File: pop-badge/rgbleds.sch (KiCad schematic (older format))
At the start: 25 parts, among them U1 WS2812-2020, U10 WS2812-2020, U11 WS2812-2020, U12 WS2812-2020, U13 WS2812-2020, U14 WS2812-2020, U15 WS2812-2020, U16 WS2812-2020, U17 WS2812-2020, U18 WS2812-2020, U19 WS2812-2020, U2 WS2812-2020, U20 WS2812-2020, U21 WS2812-2020, U22 WS2812-2020, U23 WS2812-2020, U24 WS2812-2020, U25 WS2812-2020, U3 WS2812-2020, U4 WS2812-2020, U5 WS2812-2020, U6 WS2812-2020, U7 WS2812-2020, U8 WS2812-2020, U9 WS2812-2020

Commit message: routing mostly done
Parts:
- U1, U10, U11, U12, U13, U14, U15, U16, U17, U18, U19, U2, U20, U21, U22, U23, U24, U25, U3, U4, U5, U6, U7, U8, U9: JLC (none) -> C965555
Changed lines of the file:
@@
 F 4 "Manufacturer Recommendations" H 2850 1200 50  0001 L BNN "STANDARD"
 F 5 "Worldsemi" H 2850 1200 50  0001 L BNN "MANUFACTURER"
+F 6 "C965555" H 2850 1200 50  0001 C CNN "JLC"
+F 7 "" H 2850 1200 50  0001 C CNN "LCSC"
 	1    2850 1200
 	1    0    0    -1
@@
 F 4 "Manufacturer Recommendations" H 4250 1200 50  0001 L BNN "STANDARD"
 F 5 "Worldsemi" H 4250 1200 50  0001 L BNN "MANUFACTURER"
+F 6 "C965555" H 4250 1200 50  0001 C CNN "JLC"
 	1    4250 1200
 	1    0    0    -1
@@
 F 4 "Manufacturer Recommendations" H 5650 1200 50  0001 L BNN "STANDARD"
 F 5 "Worldsemi" H 5650 1200 50  0001 L BNN "MANUFACTURER"
+F 6 "C965555" H 5650 1200 50  0001 C CNN "JLC"
 	1    5650 1200
 	1    0    0    -1
@@
 F 4 "Manufacturer Recommendations" H 7050 1200 50  0001 L BNN "STANDARD"
 F 5 "Worldsemi" H 7050 1200 50  0001 L BNN "MANUFACTURER"
+F 6 "C965555" H 7050 1200 50  0001 C CNN "JLC"
 	1    7050 1200
 	1    0    0    -1
@@
 F 4 "Manufacturer Recommendations" H 2850 2450 50  0001 L BNN "STANDARD"
 F 5 "Worldsemi" H 2850 2450 50  0001 L BNN "MANUFACTURER"
+F 6 "C965555" H 2850 2450 50  0001 C CNN "JLC"
 	1    2850 2450
 	1    0    0    -1
@@
 F 4 "Manufacturer Recommendations" H 4250 2450 50  0001 L BNN "STANDARD"
 F 5 "Worldsemi" H 4250 2450 50  0001 L BNN "MANUFACTURER"
+F 6 "C965555" H 4250 2450 50  0001 C CNN "JLC"
 	1    4250 2450
 	1    0    0    -1
@@
 F 4 "Manufacturer Recommendations" H 5650 2450 50  0001 L BNN "STANDARD"
 F 5 "Worldsemi" H 5650 2450 50  0001 L BNN "MANUFACTURER"
+F 6 "C965555" H 5650 2450 50  0001 C CNN "JLC"
 	1    5650 2450
 	1    0    0    -1
@@
 F 4 "Manufacturer Recommendations" H 7050 2450 50  0001 L BNN "STANDARD"
 F 5 "Worldsemi" H 7050 2450 50  0001 L BNN "MANUFACTURER"
+F 6 "C965555" H 7050 2450 50  0001 C CNN "JLC"
 	1    7050 2450
 	1    0    0    -1
@@
 F 4 "Manufacturer Recommendations" H 8450 2450 50  0001 L BNN "STANDARD"
 F 5 "Worldsemi" H 8450 2450 50  0001 L BNN "MANUFACTURER"
+F 6 "C965555" H 8450 2450 50  0001 C CNN "JLC"
 	1    8450 2450
 	1    0    0    -1
@@
 F 4 "Manufacturer Recommendations" H 2850 3650 50  0001 L BNN "STANDARD"
 F 5 "Worldsemi" H 2850 3650 50  0001 L BNN "MANUFACTURER"
+F 6 "C965555" H 2850 3650 50  0001 C CNN "JLC"
 	1    2850 3650
 	1    0    0    -1
@@
 F 4 "Manufacturer Recommendations" H 4250 3650 50  0001 L BNN "STANDARD"
 F 5 "Worldsemi" H 4250 3650 50  0001 L BNN "MANUFACTURER"
+F 6 "C965555" H 4250 3650 50  0001 C CNN "JLC"
 	1    4250 3650
 	1    0    0    -1
@@
 F 4 "Manufacturer Recommendations" H 5650 3650 50  0001 L BNN "STANDARD"
 F 5 "Worldsemi" H 5650 3650 50  0001 L BNN "MANUFACTURER"
+F 6 "C965555" H 5650 3650 50  0001 C CNN "JLC"
 	1    5650 3650
 	1    0    0    -1
@@
 F 4 "Manufacturer Recommendations" H 7050 3650 50  0001 L BNN "STANDARD"
 F 5 "Worldsemi" H 7050 3650 50  0001 L BNN "MANUFACTURER"
+F 6 "C965555" H 7050 3650 50  0001 C CNN "JLC"
 	1    7050 3650
 	1    0    0    -1
@@
 F 4 "Manufacturer Recommendations" H 8450 3650 50  0001 L BNN "STANDARD"
 F 5 "Worldsemi" H 8450 3650 50  0001 L BNN "MANUFACTURER"
+F 6 "C965555" H 8450 3650 50  0001 C CNN "JLC"
 	1    8450 3650
 	1    0    0    -1
@@
 F 4 "Manufacturer Recommendations" H 2850 4800 50  0001 L BNN "STANDARD"
 F 5 "Worldsemi" H 2850 4800 50  0001 L BNN "MANUFACTURER"
+F 6 "C965555" H 2850 4800 50  0001 C CNN "JLC"
 	1    2850 4800
 	1    0    0    -1
@@
 F 4 "Manufacturer Recommendations" H 4250 4800 50  0001 L BNN "STANDARD"
 F 5 "Worldsemi" H 4250 4800 50  0001 L BNN "MANUFACTURER"
+F 6 "C965555" H 4250 4800 50  0001 C CNN "JLC"
 	1    4250 4800
 	1    0    0    -1
@@
 F 4 "Manufacturer Recommendations" H 5650 4800 50  0001 L BNN "STANDARD"
 F 5 "Worldsemi" H 5650 4800 50  0001 L BNN "MANUFACTURER"
+F 6 "C965555" H 5650 4800 50  0001 C CNN "JLC"
 	1    5650 4800
 	1    0    0    -1
@@
 F 4 "Manufacturer Recommendations" H 7050 4800 50  0001 L BNN "STANDARD"
 F 5 "Worldsemi" H 7050 4800 50  0001 L BNN "MANUFACTURER"
+F 6 "C965555" H 7050 4800 50  0001 C CNN "JLC"
 	1    7050 4800
 	1    0    0    -1
@@
 F 4 "Manufacturer Recommendations" H 8450 4800 50  0001 L BNN "STANDARD"
 F 5 "Worldsemi" H 8450 4800 50  0001 L BNN "MANUFACTURER"
+F 6 "C965555" H 8450 4800 50  0001 C CNN "JLC"
 	1    8450 4800
 	1    0    0    -1
@@
 F 4 "Manufacturer Recommendations" H 2850 5950 50  0001 L BNN "STANDARD"
 F 5 "Worldsemi" H 2850 5950 50  0001 L BNN "MANUFACTURER"
+F 6 "C965555" H 2850 5950 50  0001 C CNN "JLC"
 	1    2850 5950
 	1    0    0    -1
@@
 F 4 "Manufacturer Recommendations" H 4250 5950 50  0001 L BNN "STANDARD"
 F 5 "Worldsemi" H 4250 5950 50  0001 L BNN "MANUFACTURER"
+F 6 "C965555" H 4250 5950 50  0001 C CNN "JLC"
 	1    4250 5950
 	1    0    0    -1
@@
 F 4 "Manufacturer Recommendations" H 5650 5950 50  0001 L BNN "STANDARD"
 F 5 "Worldsemi" H 5650 5950 50  0001 L BNN "MANUFACTURER"
+F 6 "C965555" H 5650 5950 50  0001 C CNN "JLC"
 	1    5650 5950
 	1    0    0    -1
@@
 F 4 "Manufacturer Recommendations" H 7050 5950 50  0001 L BNN "STANDARD"
 F 5 "Worldsemi" H 7050 5950 50  0001 L BNN "MANUFACTURER"
+F 6 "C965555" H 7050 5950 50  0001 C CNN "JLC"
 	1    7050 5950
 	1    0    0    -1
@@
 F 4 "Manufacturer Recommendations" H 8450 5950 50  0001 L BNN "STANDARD"
 F 5 "Worldsemi" H 8450 5950 50  0001 L BNN "MANUFACTURER"
+F 6 "C965555" H 8450 5950 50  0001 C CNN "JLC"
 	1    8450 5950
 	1    0    0    -1
@@
 F 4 "Manufacturer Recommendations" H 8450 1200 50  0001 L BNN "STANDARD"
 F 5 "Worldsemi" H 8450 1200 50  0001 L BNN "MANUFACTURER"
+F 6 "C965555" H 8450 1200 50  0001 C CNN "JLC"
 	1    8450 1200
 	1    0    0    -1

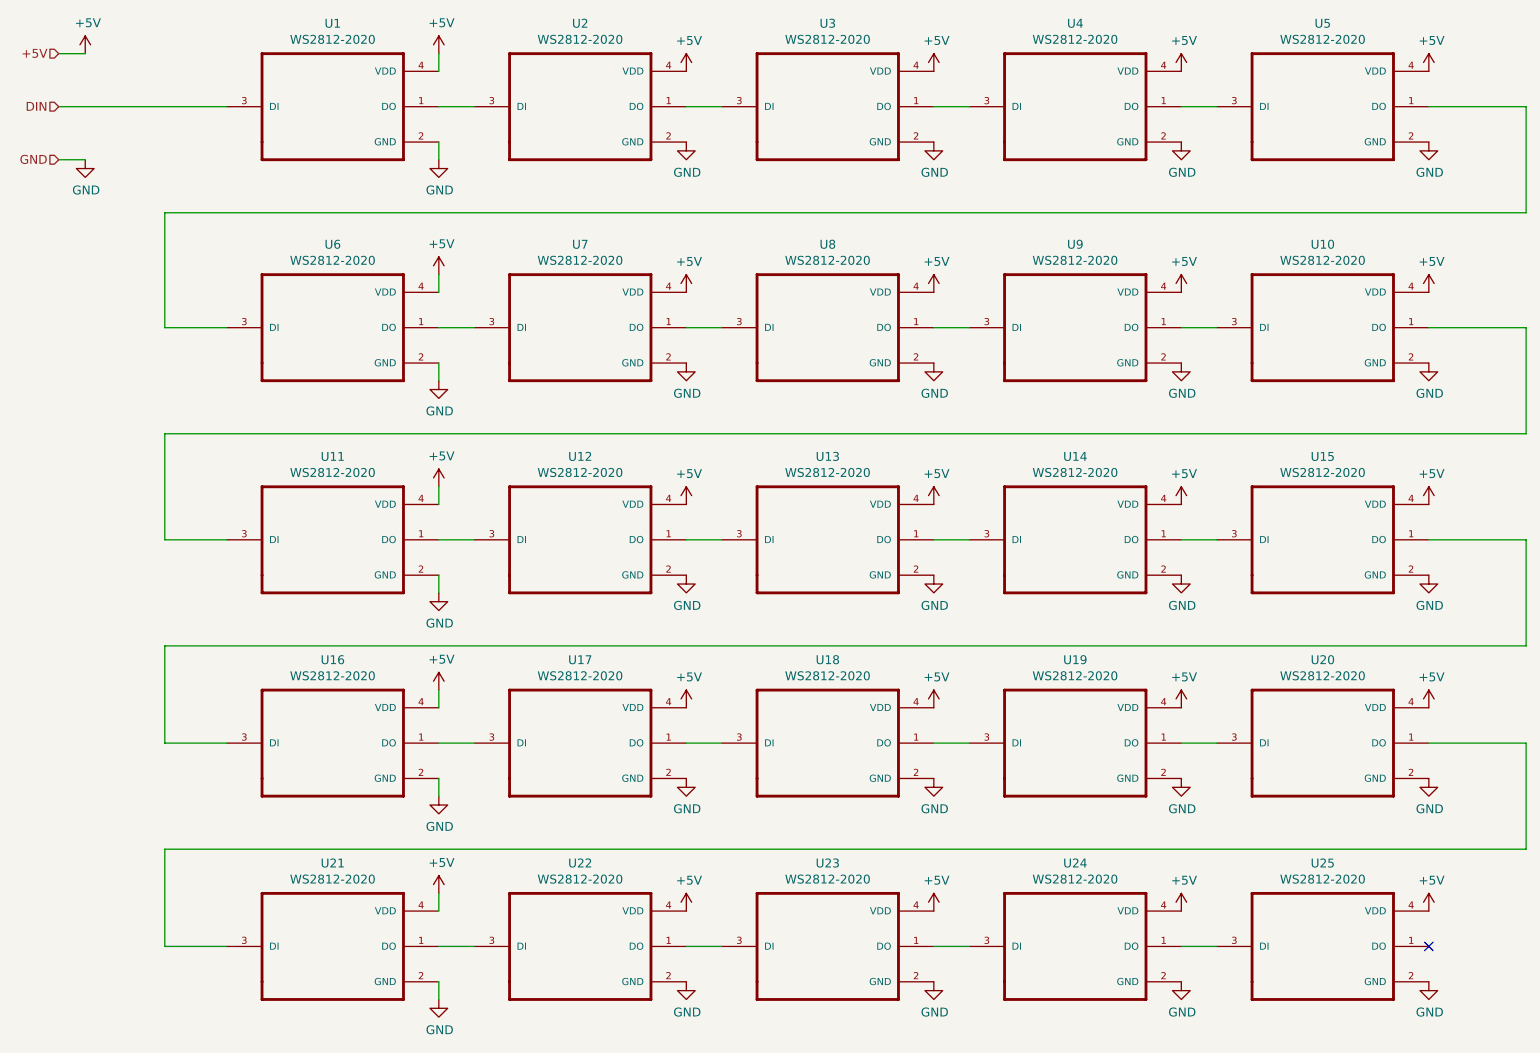
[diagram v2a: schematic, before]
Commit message: add WS2812B 2020 decoupling caps (100nF)
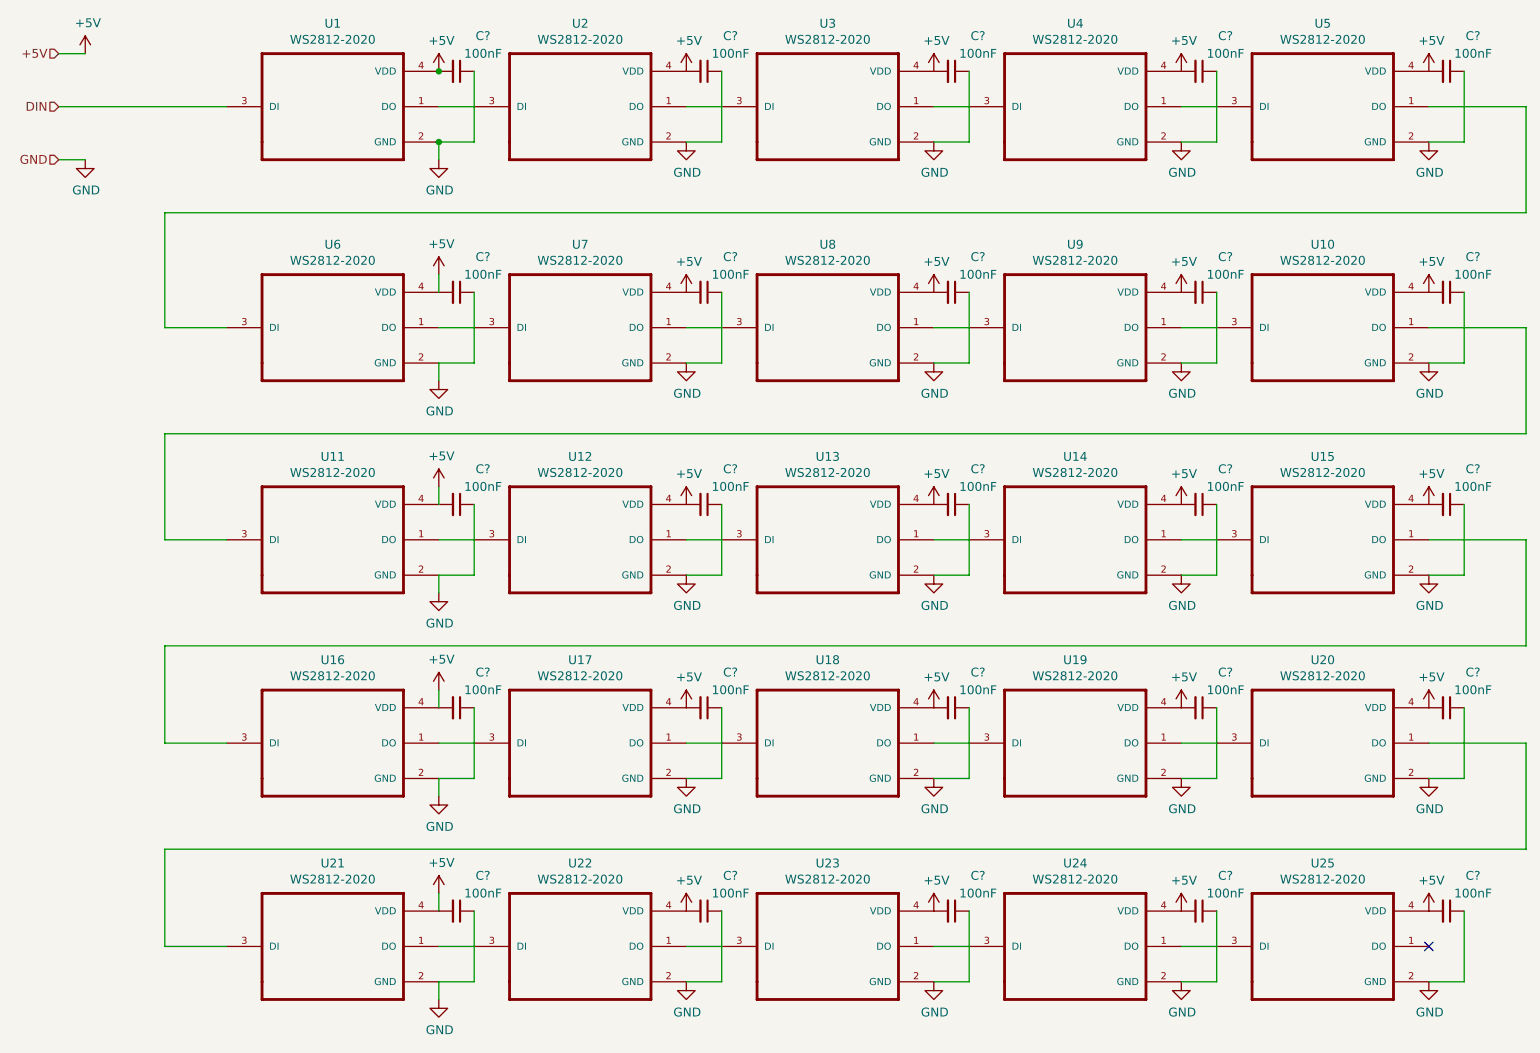
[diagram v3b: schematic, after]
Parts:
- added C? (x25): 100nF, symbol Device:C_Small
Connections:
- net +5V: now also C?.2, C?.2, C?.2, C?.2, C?.2, C?.2, C?.2, C?.2, C?.2, C?.2, C?.2, C?.2, C?.2, C?.2, C?.2, C?.2, C?.2, C?.2, C?.2, C?.2, C?.2, C?.2, C?.2, C?.2, C?.2
- net GND: now also C?.1, C?.1, C?.1, C?.1, C?.1, C?.1, C?.1, C?.1, C?.1, C?.1, C?.1, C?.1, C?.1, C?.1, C?.1, C?.1, C?.1, C?.1, C?.1, C?.1, C?.1, C?.1, C?.1, C?.1, C?.1

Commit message: annotate decoupling caps
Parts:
- gave numbers to parts that had none: 25
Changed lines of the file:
@@
 $EndComp
 $Comp
-L Device:C_Small C?
+L Device:C_Small C1
 U 1 1 619E0098
 P 3550 1000
-F 0 "C?" V 3350 1150 50  0000 C CNN
+F 0 "C1" V 3350 1150 50  0000 C CNN
 F 1 "100nF" V 3450 1150 50  0000 C CNN
 F 2 "" H 3550 1000 50  0001 C CNN
@@
 Connection ~ 3450 1400
 $Comp
-L Device:C_Small C?
+L Device:C_Small C3
 U 1 1 619FC1C9
 P 6350 1000
-F 0 "C?" V 6150 1150 50  0000 C CNN
+F 0 "C3" V 6150 1150 50  0000 C CNN
 F 1 "100nF" V 6250 1150 50  0000 C CNN
 F 2 "" H 6350 1000 50  0001 C CNN
@@
 	3650 1000 3650 1400
 $Comp
-L Device:C_Small C?
+L Device:C_Small C2
 U 1 1 61A0DF82
 P 4950 1000
-F 0 "C?" V 4750 1150 50  0000 C CNN
+F 0 "C2" V 4750 1150 50  0000 C CNN
 F 1 "100nF" V 4850 1150 50  0000 C CNN
 F 2 "" H 4950 1000 50  0001 C CNN
@@
 	5050 1400 4850 1400
 $Comp
-L Device:C_Small C?
+L Device:C_Small C4
 U 1 1 61A14188
 P 7750 1000
-F 0 "C?" V 7550 1150 50  0000 C CNN
+F 0 "C4" V 7550 1150 50  0000 C CNN
 F 1 "100nF" V 7650 1150 50  0000 C CNN
 F 2 "" H 7750 1000 50  0001 C CNN
@@
 	7850 1400 7650 1400
 $Comp
-L Device:C_Small C?
+L Device:C_Small C5
 U 1 1 61A15807
 P 9150 1000
-F 0 "C?" V 8950 1150 50  0000 C CNN
+F 0 "C5" V 8950 1150 50  0000 C CNN
 F 1 "100nF" V 9050 1150 50  0000 C CNN
 F 2 "" H 9150 1000 50  0001 C CNN
@@
 	9250 1400 9050 1400
 $Comp
-L Device:C_Small C?
+L Device:C_Small C10
 U 1 1 61A16E85
 P 9150 2250
-F 0 "C?" V 8950 2400 50  0000 C CNN
+F 0 "C10" V 8950 2400 50  0000 C CNN
 F 1 "100nF" V 9050 2400 50  0000 C CNN
 F 2 "" H 9150 2250 50  0001 C CNN
@@
 	9250 2650 9050 2650
 $Comp
-L Device:C_Small C?
+L Device:C_Small C9
 U 1 1 61A1872E
 P 7750 2250
-F 0 "C?" V 7550 2400 50  0000 C CNN
+F 0 "C9" V 7550 2400 50  0000 C CNN
 F 1 "100nF" V 7650 2400 50  0000 C CNN
 F 2 "" H 7750 2250 50  0001 C CNN
@@
 	7850 2650 7650 2650
 $Comp
-L Device:C_Small C?
+L Device:C_Small C8
 U 1 1 61A1A012
 P 6350 2250
-F 0 "C?" V 6150 2400 50  0000 C CNN
+F 0 "C8" V 6150 2400 50  0000 C CNN
 F 1 "100nF" V 6250 2400 50  0000 C CNN
 F 2 "" H 6350 2250 50  0001 C CNN
@@
 	6450 2650 6250 2650
 $Comp
-L Device:C_Small C?
+L Device:C_Small C7
 U 1 1 61A1BB70
 P 4950 2250
-F 0 "C?" V 4750 2400 50  0000 C CNN
+F 0 "C7" V 4750 2400 50  0000 C CNN
 F 1 "100nF" V 4850 2400 50  0000 C CNN
 F 2 "" H 4950 2250 50  0001 C CNN
@@
 	5050 2650 4850 2650
 $Comp
-L Device:C_Small C?
+L Device:C_Small C12
 U 1 1 61A1D8BD
 P 4950 3450
-F 0 "C?" V 4750 3600 50  0000 C CNN
+F 0 "C12" V 4750 3600 50  0000 C CNN
 F 1 "100nF" V 4850 3600 50  0000 C CNN
 F 2 "" H 4950 3450 50  0001 C CNN
@@
 	5050 3850 4850 3850
 $Comp
-L Device:C_Small C?
+L Device:C_Small C13
 U 1 1 61A1F611
 P 6350 3450
-F 0 "C?" V 6150 3600 50  0000 C CNN
+F 0 "C13" V 6150 3600 50  0000 C CNN
 F 1 "100nF" V 6250 3600 50  0000 C CNN
 F 2 "" H 6350 3450 50  0001 C CNN
@@
 	6450 3850 6250 3850
 $Comp
-L Device:C_Small C?
+L Device:C_Small C14
 U 1 1 61A21406
 P 7750 3450
-F 0 "C?" V 7550 3600 50  0000 C CNN
+F 0 "C14" V 7550 3600 50  0000 C CNN
 F 1 "100nF" V 7650 3600 50  0000 C CNN
 F 2 "" H 7750 3450 50  0001 C CNN
@@
 	7850 3850 7650 3850
 $Comp
-L Device:C_Small C?
+L Device:C_Small C15
 U 1 1 61A233C0
 P 9150 3450
-F 0 "C?" V 8950 3600 50  0000 C CNN
+F 0 "C15" V 8950 3600 50  0000 C CNN
 F 1 "100nF" V 9050 3600 50  0000 C CNN
 F 2 "" H 9150 3450 50  0001 C CNN
@@
 	9250 3850 9050 3850
 $Comp
-L Device:C_Small C?
+L Device:C_Small C6
 U 1 1 61A253A1
 P 3550 2250
-F 0 "C?" V 3350 2400 50  0000 C CNN
+F 0 "C6" V 3350 2400 50  0000 C CNN
 F 1 "100nF" V 3450 2400 50  0000 C CNN
 F 2 "" H 3550 2250 50  0001 C CNN
@@
 	3650 2650 3450 2650
 $Comp
-L Device:C_Small C?
+L Device:C_Small C11
 U 1 1 61A27454
 P 3550 3450
-F 0 "C?" V 3350 3600 50  0000 C CNN
+F 0 "C11" V 3350 3600 50  0000 C CNN
 F 1 "100nF" V 3450 3600 50  0000 C CNN
 F 2 "" H 3550 3450 50  0001 C CNN
@@
 	3650 3850 3450 3850
 $Comp
-L Device:C_Small C?
+L Device:C_Small C25
 U 1 1 61A2AD40
 P 9150 5750
-F 0 "C?" V 8950 5900 50  0000 C CNN
+F 0 "C25" V 8950 5900 50  0000 C CNN
 F 1 "100nF" V 9050 5900 50  0000 C CNN
 F 2 "" H 9150 5750 50  0001 C CNN
@@
 	9250 6150 9050 6150
 $Comp
-L Device:C_Small C?
+L Device:C_Small C20
 U 1 1 61A2D09E
 P 9150 4600
-F 0 "C?" V 8950 4750 50  0000 C CNN
+F 0 "C20" V 8950 4750 50  0000 C CNN
 F 1 "100nF" V 9050 4750 50  0000 C CNN
 F 2 "" H 9150 4600 50  0001 C CNN
@@
 	9250 5000 9050 5000
 $Comp
-L Device:C_Small C?
+L Device:C_Small C19
 U 1 1 61A2F5B2
 P 7750 4600
-F 0 "C?" V 7550 4750 50  0000 C CNN
+F 0 "C19" V 7550 4750 50  0000 C CNN
 F 1 "100nF" V 7650 4750 50  0000 C CNN
 F 2 "" H 7750 4600 50  0001 C CNN
@@
 	7850 5000 7650 5000
 $Comp
-L Device:C_Small C?
+L Device:C_Small C18
 U 1 1 61A31AB9
 P 6350 4600
-F 0 "C?" V 6150 4750 50  0000 C CNN
+F 0 "C18" V 6150 4750 50  0000 C CNN
 F 1 "100nF" V 6250 4750 50  0000 C CNN
 F 2 "" H 6350 4600 50  0001 C CNN
@@
 	6450 5000 6250 5000
 $Comp
-L Device:C_Small C?
+L Device:C_Small C24
 U 1 1 61A35DA2
 P 7750 5750
-F 0 "C?" V 7550 5900 50  0000 C CNN
+F 0 "C24" V 7550 5900 50  0000 C CNN
 F 1 "100nF" V 7650 5900 50  0000 C CNN
 F 2 "" H 7750 5750 50  0001 C CNN
@@
 	7850 6150 7650 6150
 $Comp
-L Device:C_Small C?
+L Device:C_Small C23
 U 1 1 61A386B3
 P 6350 5750
-F 0 "C?" V 6150 5900 50  0000 C CNN
+F 0 "C23" V 6150 5900 50  0000 C CNN
 F 1 "100nF" V 6250 5900 50  0000 C CNN
 F 2 "" H 6350 5750 50  0001 C CNN
@@
 	6450 6150 6250 6150
 $Comp
-L Device:C_Small C?
+L Device:C_Small C22
 U 1 1 61A3B137
 P 4950 5750
-F 0 "C?" V 4750 5900 50  0000 C CNN
+F 0 "C22" V 4750 5900 50  0000 C CNN
 F 1 "100nF" V 4850 5900 50  0000 C CNN
 F 2 "" H 4950 5750 50  0001 C CNN
@@
 	5050 6150 4850 6150
 $Comp
-L Device:C_Small C?
+L Device:C_Small C21
 U 1 1 61A3DDC2
 P 3550 5750
-F 0 "C?" V 3350 5900 50  0000 C CNN
+F 0 "C21" V 3350 5900 50  0000 C CNN
 F 1 "100nF" V 3450 5900 50  0000 C CNN
 F 2 "" H 3550 5750 50  0001 C CNN
@@
 	3650 6150 3450 6150
 $Comp
-L Device:C_Small C?
+L Device:C_Small C16
 U 1 1 61A40CB3
 P 3550 4600
-F 0 "C?" V 3350 4750 50  0000 C CNN
+F 0 "C16" V 3350 4750 50  0000 C CNN
 F 1 "100nF" V 3450 4750 50  0000 C CNN
 F 2 "" H 3550 4600 50  0001 C CNN
@@
 	3650 5000 3450 5000
 $Comp
-L Device:C_Small C?
+L Device:C_Small C17
 U 1 1 61A43D1F
 P 4950 4600
-F 0 "C?" V 4750 4750 50  0000 C CNN
+F 0 "C17" V 4750 4750 50  0000 C CNN
 F 1 "100nF" V 4850 4750 50  0000 C CNN
 F 2 "" H 4950 4600 50  0001 C CNN
